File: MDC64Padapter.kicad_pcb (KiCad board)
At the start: 2 copper layers, 42.7 x 31 mm, 36 parts, among them J1 DB9_F_TO_C64, J2 DB9_M_TO_PAD, Q1 BC847, Q2 BC847, SW1 MODE, U1 74ACT08, U2 74ACT373, U3 74ACT157, U4 74ACT373, U5 74AHC1G04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

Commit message: First rev of the board
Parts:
- moved C7 0.47 mm to (84.9, 102.1)
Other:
- board text added: "5x 1N4148"
- board text added: "MODE A"
- board text added: "MODE B"

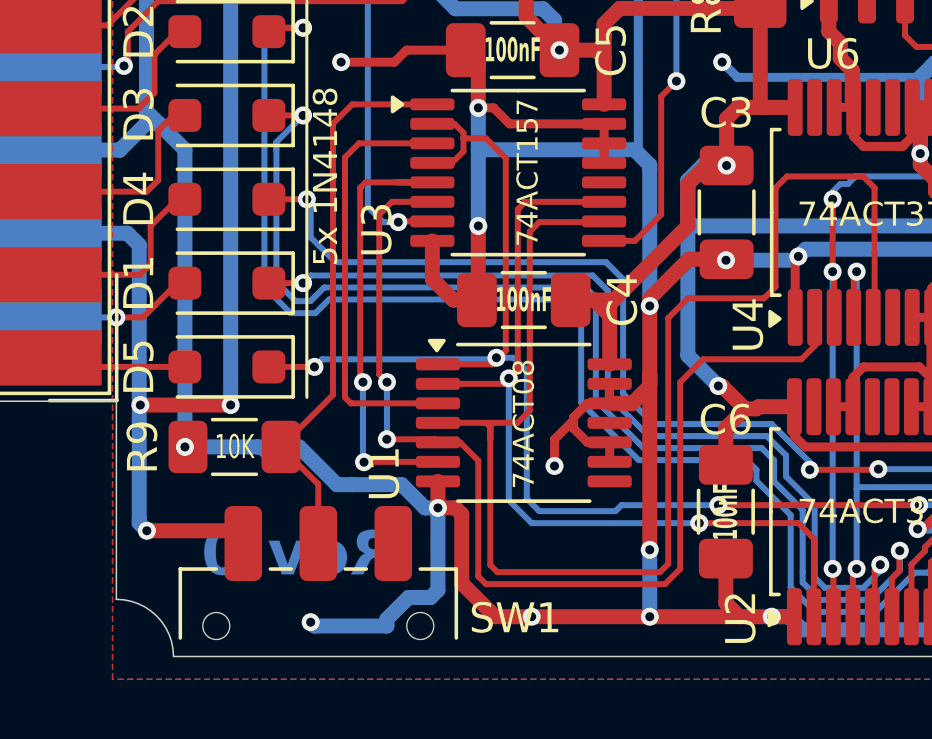
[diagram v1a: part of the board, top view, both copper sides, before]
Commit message: Change the silkscreen
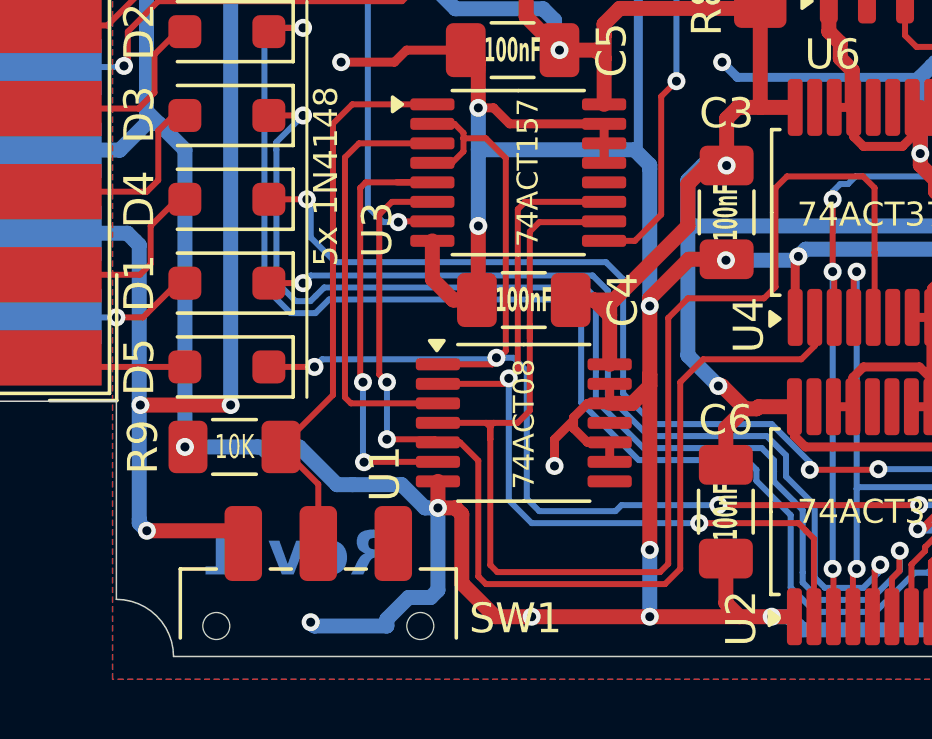
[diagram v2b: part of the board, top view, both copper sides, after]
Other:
- board text added: "Rev.1"
- board text removed: "Rev.0"
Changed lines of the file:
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@@
 		)
 		(property "Value" "100nF"
-			(at 0 1.85 90)
-			(layer "F.Fab")
+			(at 0 0.022 90)
+			(layer "F.SilkS")
 			(effects
 				(font
-					(size 1 1)
-					(thickness 0.15)
+					(size 0.8 0.4)
+					(thickness 0.08)
+					(bold yes)
 				)
 			)
@@
 		)
 		(property "Value" "10uF"
-			(at 0 0 270)
+			(at 0 0 -90)
 			(layer "F.SilkS")
 			(effects
@@
 		(layer "Edge.Cuts")
 	)
-	(gr_text "Rev.0"
+	(gr_text "Rev.1"
 		(at 65.151 128.397 0)
 		(layer "B.Cu")

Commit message: Fix c64 up signal traces on PCB
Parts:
- C1: value 10uF -> 10nF
- R7: value 47K -> 10K
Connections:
- J2 pad 1: /C64_UP -> /MD_UP
- RN1 pad 5: /C64_UP -> /MD_UP
- U1 pad 1: /C64_UP -> /MD_UP
- U3 pad 2: /C64_UP -> /MD_UP
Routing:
- net /MD_UP: track 0.00 -> 45.7 mm, vias 0 -> 4
- net /C64_UP: track 54.8 -> 11.8 mm, vias 5 -> 2
- net Net-(U3-I0b): track 15.3 -> 13.9 mm

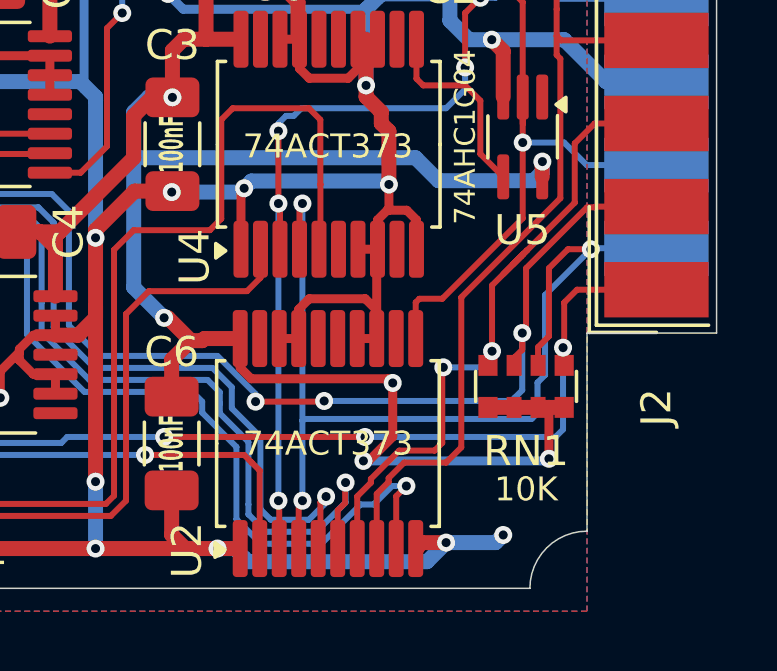
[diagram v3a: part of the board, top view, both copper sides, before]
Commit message: Add filter caps for up/down direction
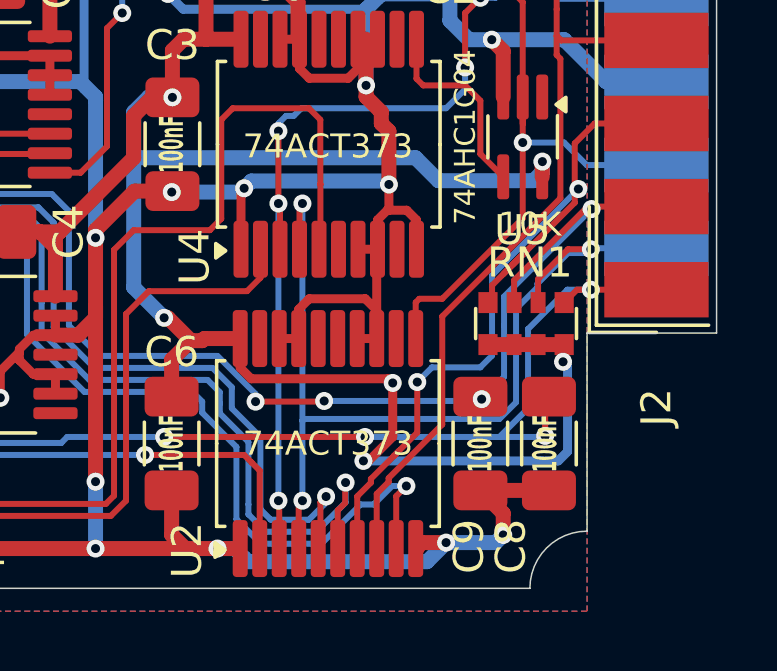
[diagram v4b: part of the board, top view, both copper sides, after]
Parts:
- added C8: 100nF, Capacitor_SMD:C_1206_3216Metric_Pad1.33x1.80mm_HandSolder, F.Cu at (91.9, 127.0)
- added C9: 100nF, Capacitor_SMD:C_1206_3216Metric_Pad1.33x1.80mm_HandSolder, F.Cu at (89.7, 127.0)
- moved RN1 2.09 mm to (91.2, 123.0)
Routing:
- net /MD_LEFT_M: track 22.7 -> 27.4 mm
- net GND: track 248.0 -> 252.1 mm
- net /MD_UP: track 45.7 -> 48.8 mm, vias 4 -> 5
- net VCC: track 166.2 -> 168.9 mm
- net /C64_DOWN: track 44.6 -> 47.1 mm, vias 4 -> 5
- net /MD_B/~{A}: track 34.5 -> 32.2 mm
- net /MD_RIGHT_M: track 28.7 -> 27.9 mm

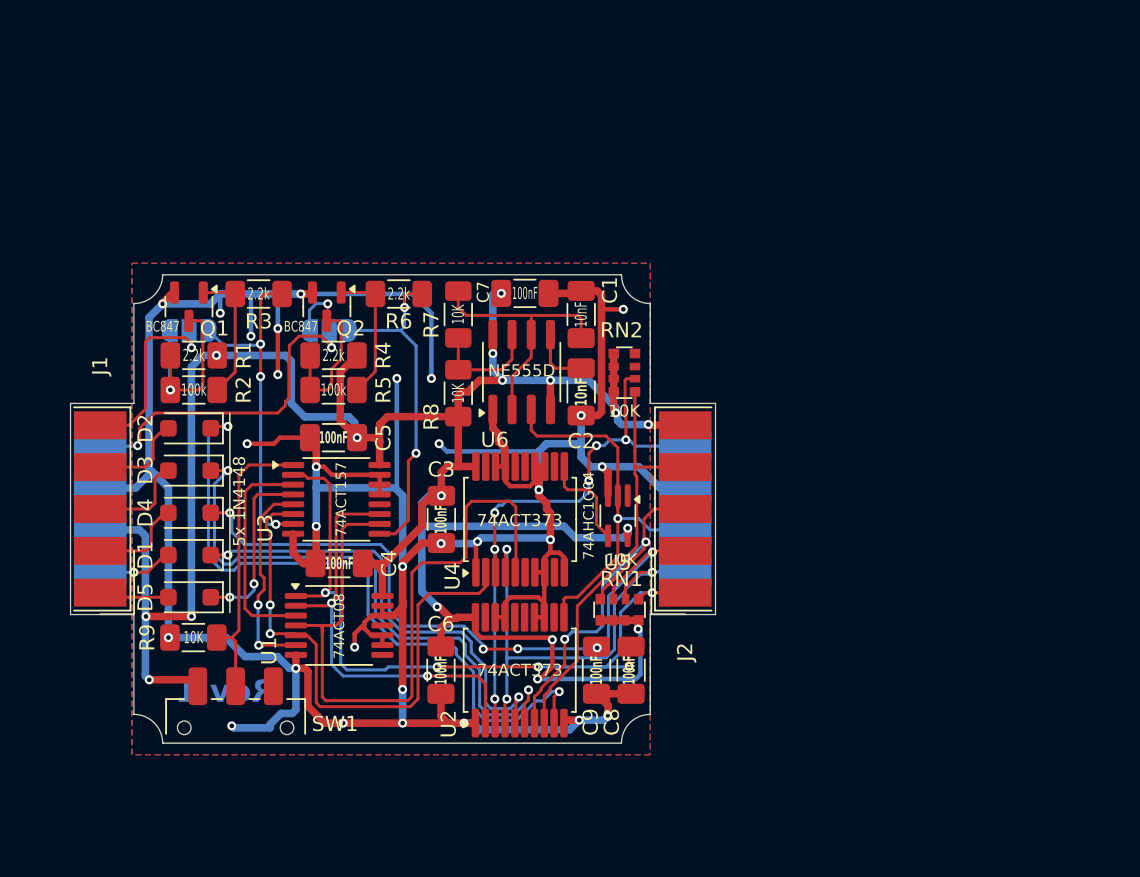
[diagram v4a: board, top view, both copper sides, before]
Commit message: Begin reorganizing the board
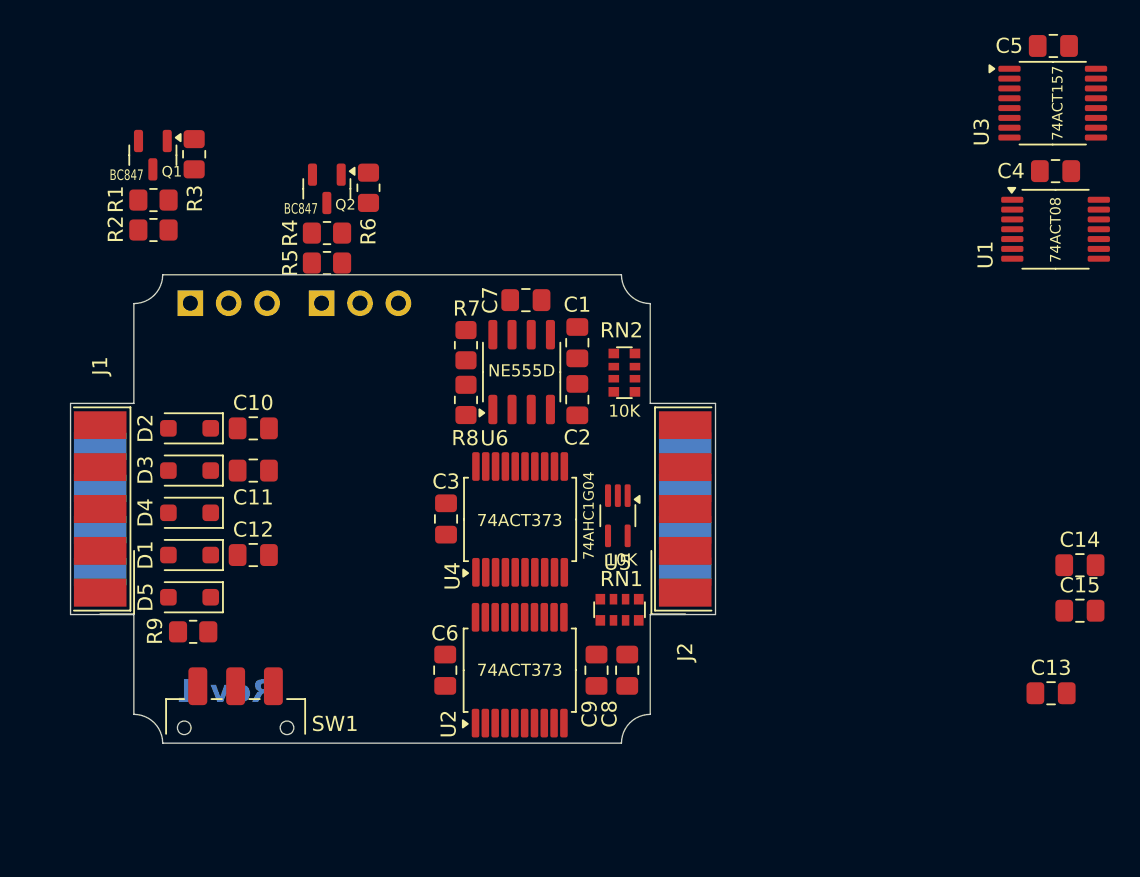
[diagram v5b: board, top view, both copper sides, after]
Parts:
- added C10: 100nF, Capacitor_SMD:C_0805_2012Metric_Pad1.18x1.45mm_HandSolder, F.Cu at (67.0, 111.0)
- added C11: 100nF, Capacitor_SMD:C_0805_2012Metric_Pad1.18x1.45mm_HandSolder, F.Cu at (67.0, 113.8)
- added C12: 100nF, Capacitor_SMD:C_0805_2012Metric_Pad1.18x1.45mm_HandSolder, F.Cu at (67.0, 119.4)
- added C13: 100nF, Capacitor_SMD:C_0805_2012Metric_Pad1.18x1.45mm_HandSolder, F.Cu at (119.7, 128.5)
- added C14: 100nF, Capacitor_SMD:C_0805_2012Metric_Pad1.18x1.45mm_HandSolder, F.Cu at (121.6, 120.1)
- added C15: 100nF, Capacitor_SMD:C_0805_2012Metric_Pad1.18x1.45mm_HandSolder, F.Cu at (121.6, 123.1)
- C1, C2, C3, C4, C5, C6, C7, C8, C9: footprint Capacitor_SMD:C_1206_3216Metric_Pad1.33x1.80mm_HandSolder -> Capacitor_SMD:C_0805_2012Metric_Pad1.18x1.45mm_HandSolder
- JP1, JP2: footprint Jumper:SolderJumper-3_P1.3mm_Open_RoundedPad1.0x1.5mm -> Connector_PinHeader_2.54mm:PinHeader_1x03_P2.54mm_Vertical
- R1, R2, R3, R4, R5, R6, R7, R8, R9: footprint Resistor_SMD:R_1206_3216Metric_Pad1.30x1.75mm_HandSolder -> Resistor_SMD:R_0805_2012Metric_Pad1.20x1.40mm_HandSolder
- moved C5 54.2 mm to (119.9, 85.7)
- moved U1 54.2 mm to (120.0, 97.8)
- moved U3 54.2 mm to (119.8, 89.5)
- moved C4 54.0 mm to (120.0, 94.0)
- moved R2 10.9 mm to (60.4, 97.9)
- moved R1 10.6 mm to (60.4, 95.9)
- moved Q1 10.3 mm to (60.3, 92.9)
- moved R3 10.2 mm to (63.0, 92.9), turned to 90 degrees
- moved R5 8.41 mm to (71.8, 100.1)
- moved R4 8.10 mm to (71.8, 98.1)
- moved Q2 7.80 mm to (71.8, 95.2)
- moved R6 7.31 mm to (74.6, 95.1), turned to 90 degrees
- moved R7 2.09 mm to (81.0, 105.5)
- moved C1 1.88 mm to (88.4, 105.3)
- moved JP2 1.87 mm to (71.5, 102.7), turned to -90 degrees
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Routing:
- net GND: track 252.1 -> 0.00 mm, vias 30 -> 0
- net VCC: track 168.9 -> 0.00 mm, vias 17 -> 0
- net /MD_UP: track 48.8 -> 0.00 mm, vias 5 -> 0
- net /MD_A: track 47.3 -> 0.00 mm
- net /C64_DOWN: track 47.1 -> 0.00 mm, vias 5 -> 0
- net /C64_RIGHT: track 45.5 -> 0.00 mm, vias 2 -> 0
- net /C64_LEFT: track 39.8 -> 0.00 mm, vias 2 -> 0
- net /MD_C/~{ST}: track 36.5 -> 0.00 mm, vias 6 -> 0
- net /MD_START: track 36.0 -> 0.00 mm, vias 2 -> 0
- net /MD_B/~{A}: track 32.2 -> 0.00 mm, vias 3 -> 0
- net /C64_FIRE: track 30.9 -> 0.00 mm, vias 2 -> 0
- net /MD_C: track 28.5 -> 0.00 mm, vias 2 -> 0
- net /MD_RIGHT_M: track 27.9 -> 0.00 mm
- net /MD_LEFT_M: track 27.4 -> 0.00 mm, vias 2 -> 0
- net /CLK: track 26.4 -> 0.00 mm, vias 1 -> 0
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- removed copper zone on B.Cu, net GND
- removed copper zone on F.Cu, net GND
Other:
- board text removed: "5x 1N4148"

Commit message: Reorganize the board a bit
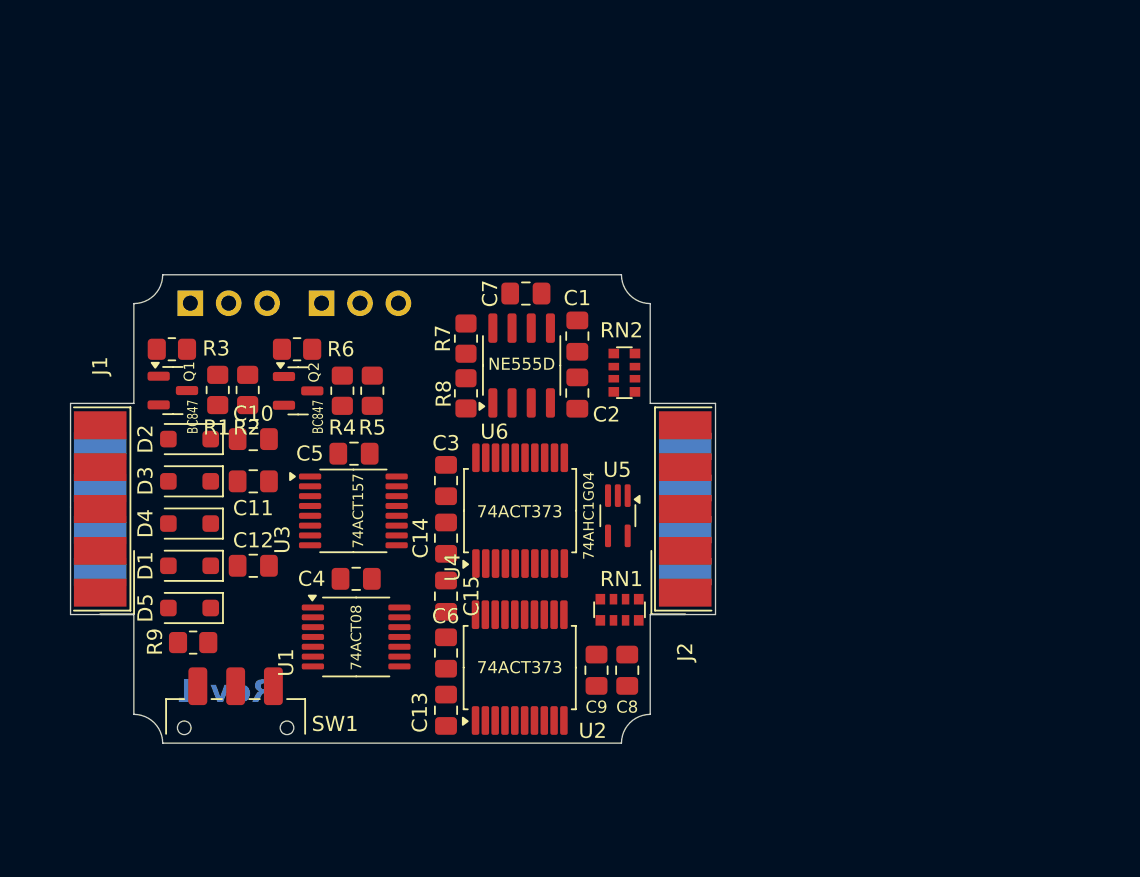
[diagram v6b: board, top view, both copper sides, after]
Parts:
- moved C4 53.6 mm to (73.8, 121.0)
- moved C5 53.6 mm to (73.6, 112.7)
- moved U1 53.6 mm to (73.8, 124.8)
- moved U3 53.6 mm to (73.6, 116.5)
- moved C14 42.0 mm to (79.7, 118.3), turned to 90 degrees
- moved C15 42.0 mm to (79.7, 122.1), turned to -90 degrees
- moved C13 40.0 mm to (79.7, 129.6), turned to -90 degrees
- moved Q1 15.6 mm to (61.6, 108.5), turned to 0 degrees
- moved Q2 13.5 mm to (69.9, 108.5), turned to 0 degrees
- moved R1 13.3 mm to (64.6, 108.5), turned to -90 degrees
- moved R3 13.0 mm to (61.6, 105.8), turned to 180 degrees
- moved R2 12.3 mm to (66.6, 108.5), turned to -90 degrees
- moved R6 11.7 mm to (69.8, 105.8), turned to 180 degrees
- moved R4 10.5 mm to (72.8, 108.5), turned to -90 degrees
- moved R5 8.96 mm to (74.8, 108.5), turned to -90 degrees
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
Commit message: Reroute the adapter
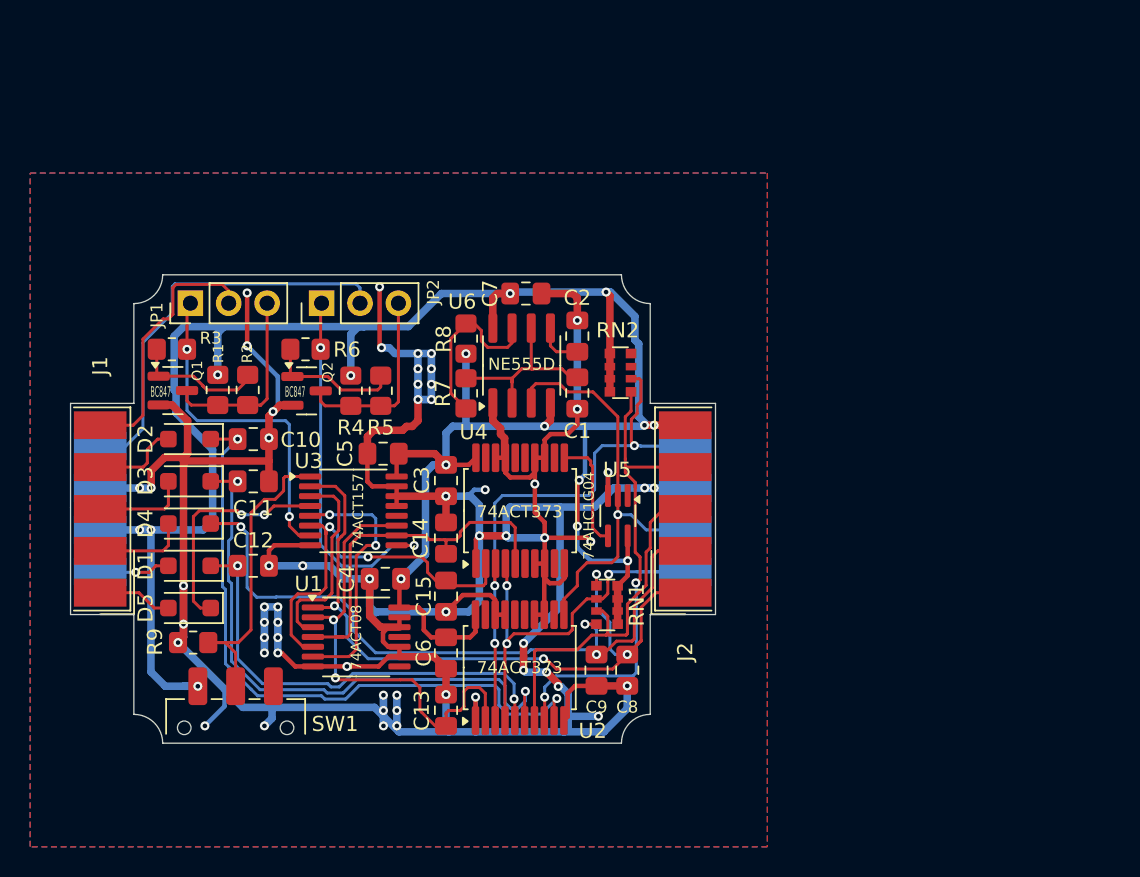
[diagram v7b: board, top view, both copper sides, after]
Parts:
- JP1, JP2: moved to F.Cu
- moved C1 3.77 mm to (88.4, 108.7), turned to 90 degrees
- moved C2 3.77 mm to (88.4, 104.9), turned to -90 degrees
- moved R7 3.62 mm to (81.0, 108.7)
- moved R8 3.62 mm to (81.0, 105.1)
- moved C4 1.93 mm to (75.7, 121.0)
- moved C5 1.93 mm to (75.5, 112.7)
- moved RN1 0.89 mm to (90.4, 122.7), turned to 180 degrees
- moved Q2 0.56 mm to (70.5, 108.5)
- moved R4 0.56 mm to (73.4, 108.5)
- moved R5 0.56 mm to (75.4, 108.5)
- moved R6 0.56 mm to (70.4, 105.8)
- moved RN2 0.26 mm to (91.2, 107.3)
- turned C13 to 90 degrees
- turned JP1 to 90 degrees
- turned JP2 to 90 degrees
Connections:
- RN1 pad 7: /C64_DOWN -> /MD_LEFT_M
- RN1 pad 8: /MD_LEFT_M -> /C64_DOWN
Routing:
- net GND: track 0.00 -> 287.9 mm, vias 0 -> 60
- net VCC: track 0.00 -> 161.0 mm, vias 0 -> 16
- net /MD_UP: track 0.00 -> 49.0 mm, vias 0 -> 4
- net /C64_DOWN: track 0.00 -> 46.7 mm, vias 0 -> 3
- net /C64_RIGHT: track 0.00 -> 43.8 mm, vias 0 -> 2
- net /C64_LEFT: track 0.00 -> 38.9 mm, vias 0 -> 2
- net /MD_C/~{ST}: track 0.00 -> 36.8 mm, vias 0 -> 3
- net /MD_RIGHT_M: track 0.00 -> 32.2 mm, vias 0 -> 2
- net /MD_C: track 0.00 -> 31.0 mm, vias 0 -> 2
- net /C64_FIRE: track 0.00 -> 30.1 mm, vias 0 -> 2
- net /MD_B/~{A}: track 0.00 -> 28.6 mm, vias 0 -> 3
- net /CLK: track 0.00 -> 28.1 mm, vias 0 -> 1
- net /C64_POTX: track 0.00 -> 27.1 mm
- net /MD_A: track 0.00 -> 27.1 mm
- net /MD_START: track 0.00 -> 26.8 mm, vias 0 -> 2
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- added copper zone on B.Cu, net GND
- added copper zone on F.Cu, net GND
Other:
- board text removed: "Rev.1"

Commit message: build rev.1 gerbers
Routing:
- net GND: track 287.9 -> 291.4 mm
- net VCC: track 161.0 -> 162.2 mm
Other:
- board text added: "A"
- board text added: "Amiga"
- board text added: "Amiga/C64"
- board text added: "B"
- board text added: "Btn 1"
- board text added: "Btn 2"
- board text added: "Btn 3"
- board text added: "C"
- board text added: "C64"
- board text added: "MODE"
- board text added: "Megadrive Controller"
- board text added: "Mode A"
- board text added: "Mode B"
- board text added: "REV. 1"
- board text added: "START"
- board text added: "Up"
- board text removed: "MODE A"
- board text removed: "MODE B"
- board text removed: "Pins 1-2: Amiga Pins 2-3: C64"
